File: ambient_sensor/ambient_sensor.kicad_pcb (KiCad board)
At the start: 2 copper layers, 69.5 x 54 mm, 22 parts, among them J1 Conn_01x02_Pin, J2 Conn_01x02_Pin, J3 Conn_01x05_Pin, J4 Conn_01x01_Pin, J5 Conn_01x04_Pin, J6 Conn_01x02_Pin, U4 ATmega328-P, U6 LD1117S33TR_SOT223, Y1 Crystal

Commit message: everything connected but warnings
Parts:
- moved U2 157.6 mm to (248.7, 132.6), turned to 180 degrees
- moved C1 144.3 mm to (219.1, 109.2)
- moved C2 144.3 mm to (213.7, 109.2)
- moved J1 140.7 mm to (245.1, 115.5)
- moved J2 140.7 mm to (236.6, 114.2)
- moved J3 140.7 mm to (208.6, 129.8)
- moved J4 140.7 mm to (208.6, 114.8)
- moved J5 140.7 mm to (228.6, 129.8)
- moved J6 140.7 mm to (229.1, 114.2)
- moved R2 140.7 mm to (245.1, 122.3)
- moved U4 140.7 mm to (241.6, 118.0)
- moved U7 140.7 mm to (159.2, 107.7)
- moved Y1 140.7 mm to (214.1, 113.8)
- moved BT1 136.6 mm to (258.9, 137.6)
- moved C5 136.6 mm to (263.4, 127.1)
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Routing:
- net GND: track 28.1 -> 91.2 mm, vias 2 -> 1
- net +5V: track 154.7 -> 179.0 mm, vias 3 -> 1
- net SCL: track 81.0 -> 56.7 mm, vias 2 -> 0
- net SDA: track 67.3 -> 44.8 mm
- net /CS: track 16.8 -> 15.4 mm
- net Net-(U4-XTAL1/PB6): track 13.5 -> 14.5 mm

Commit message: almost all errors
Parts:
- moved J1 2.55 mm to (245.0, 118.0), turned to 180 degrees
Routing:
- net RST: track 10.7 -> 14.4 mm
- net +5V: track 179.0 -> 175.7 mm, vias 1 -> 2
- net GND: track 91.2 -> 88.7 mm
- net SCL: track 56.7 -> 57.2 mm

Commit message: almost all warnings
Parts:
- added REF**: MountingHole_2.2mm_M2, MountingHole:MountingHole_2.2mm_M2, F.Cu at (227.9, 141.8)
- added REF**: MountingHole_2.2mm_M2, MountingHole:MountingHole_2.2mm_M2, F.Cu at (166.1, 141.8)
- added REF**: MountingHole_2.2mm_M2, MountingHole:MountingHole_2.2mm_M2, F.Cu at (228.9, 94.5)
- moved U7 116.0 mm to (271.2, 138.1), turned to 0 degrees
- moved REF** 107.3 mm to (165.9, 94.2), turned to 180 degrees
- moved D1 102.0 mm to (165.0, 113.8), turned to 90 degrees
- moved C5 96.8 mm to (167.0, 118.7), turned to 0 degrees
- moved C4 96.5 mm to (167.0, 121.2), turned to 0 degrees
- moved R1 96.2 mm to (168.0, 113.7), turned to 90 degrees
- moved BT1 92.3 mm to (171.5, 108.1), turned to 0 degrees
- moved U6 82.8 mm to (174.0, 118.7), turned to 0 degrees
- moved U2 69.8 mm to (181.7, 113.1), turned to 0 degrees
- moved J1 60.4 mm to (185.4, 127.7), turned to 0 degrees
- moved R2 59.9 mm to (185.3, 123.5), turned to 90 degrees
- moved U1 56.2 mm to (220.5, 95.3), turned to 180 degrees
- moved U4 53.8 mm to (188.8, 127.8), turned to 90 degrees
- moved J2 46.2 mm to (193.8, 131.5), turned to -90 degrees
- moved U3 36.7 mm to (198.8, 113.3), turned to 0 degrees
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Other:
- outline, holes or cut-outs redrawn
- board text added: "SGP30"

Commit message: no warnings
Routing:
- net unconnected-(U7-unknown-Pad2)_1: track 0.00 -> 2.50 mm
- net unconnected-(U7-unknown-Pad1)_1: track 0.00 -> 2.50 mm

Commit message: should be ok
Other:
- board text added: "École Centrale de Lille"
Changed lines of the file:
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@@
 		(layer "Edge.Cuts")
+	)
+	(gr_text "École\nCentrale\nde Lille"
+		(at 165 134 0)
+		(layer "F.Cu")
+		(effects
+			(font
+				(size 2 2)
+				(thickness 0.5)
+				(bold yes)
+			)
+			(justify left bottom)
+		)
 	)
 	(gr_text "SGP30"

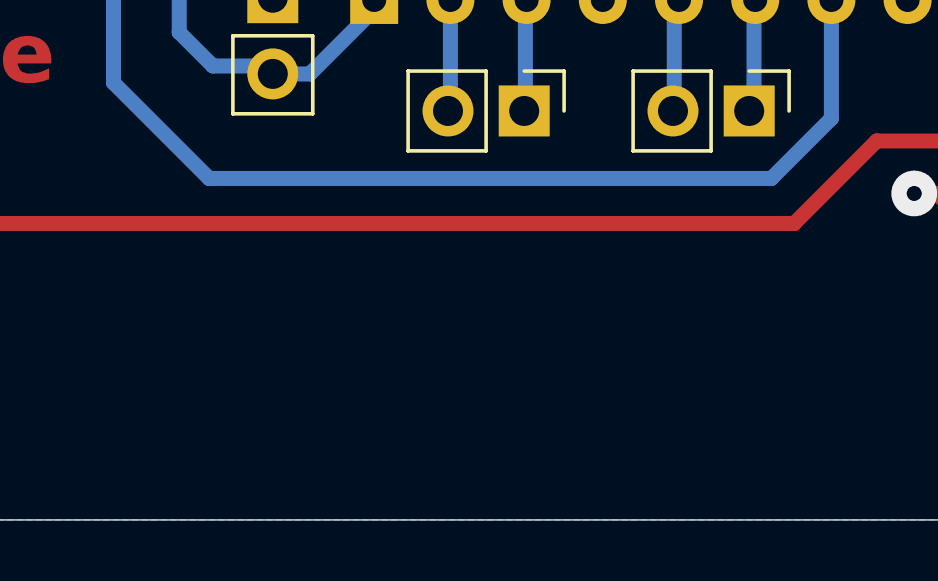
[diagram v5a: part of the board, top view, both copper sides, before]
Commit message: USB footprint
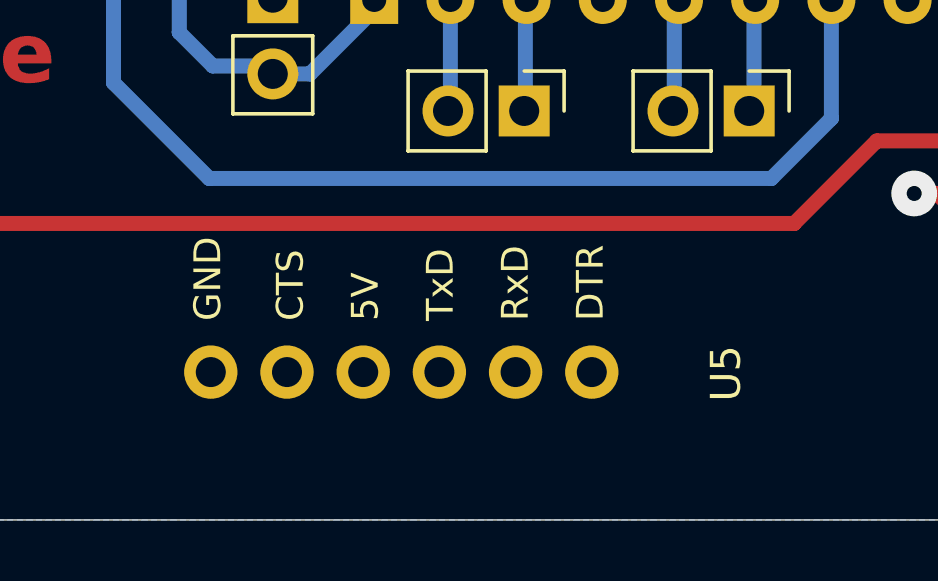
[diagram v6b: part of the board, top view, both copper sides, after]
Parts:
- added U5: ~, sensors:USB_FTDI_GT1125, F.Cu at (201.0, 140.2)
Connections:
- net Net-(J2-Pin_1) renamed /TX
- net Net-(J2-Pin_2) renamed /RX
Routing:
- net unconnected-(U7-unknown-Pad1)_1: track 0.00 -> 2.50 mm
- net unconnected-(U7-unknown-Pad1): track 2.50 -> 0.00 mm

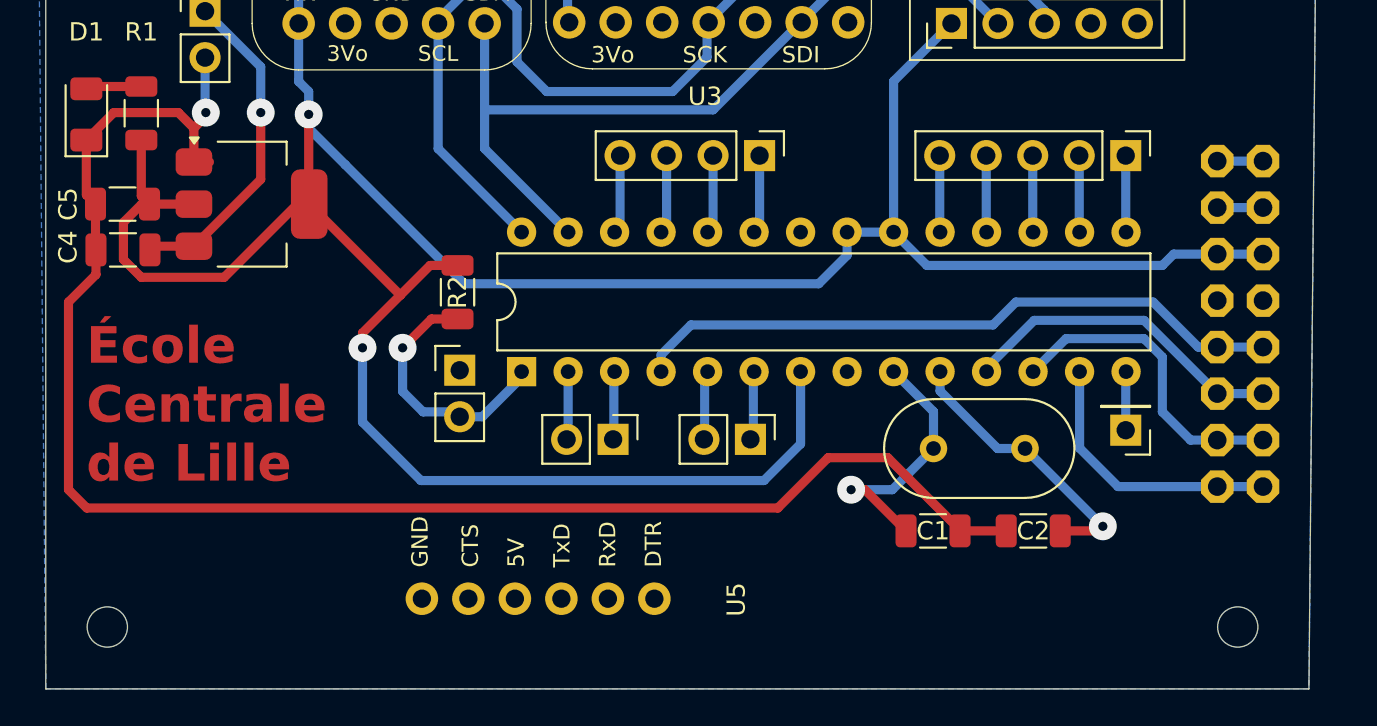
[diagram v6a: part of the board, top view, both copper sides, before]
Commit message: USB in the PCB
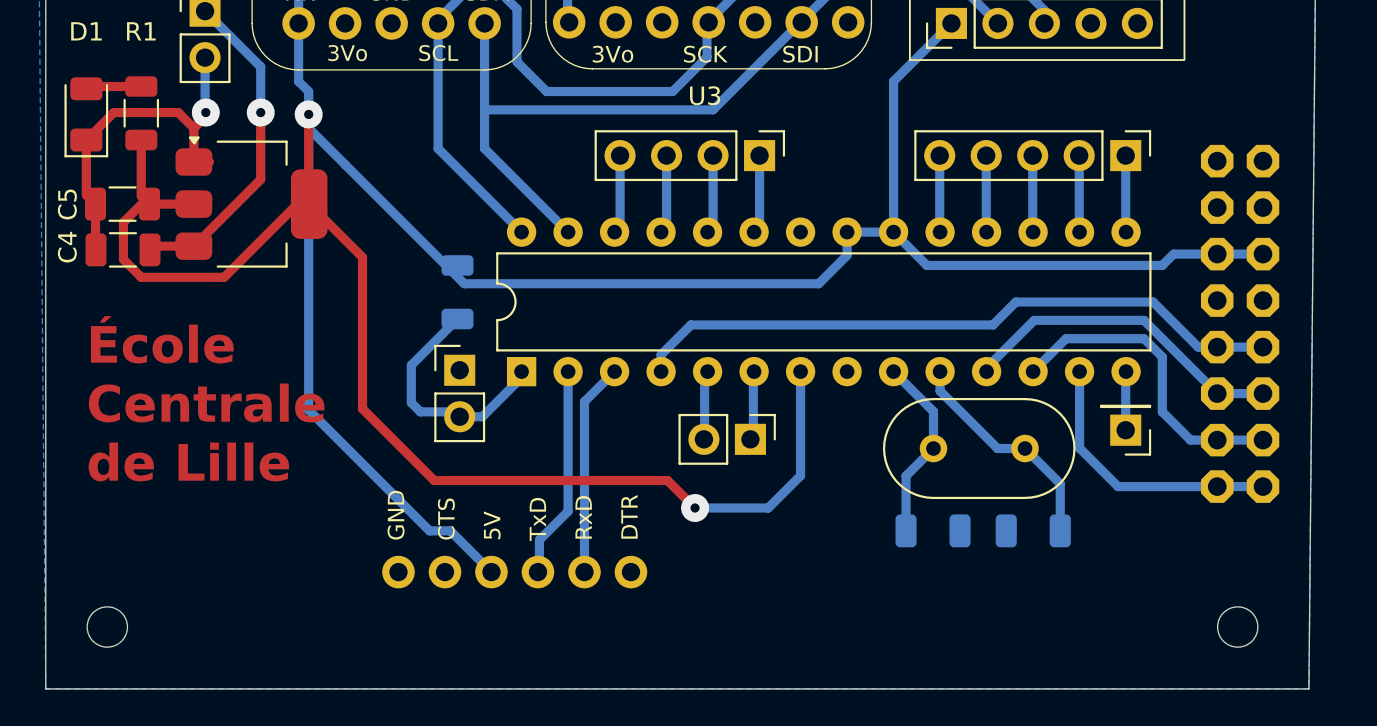
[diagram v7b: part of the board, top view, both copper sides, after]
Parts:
- removed J2: Conn_01x02_Pin, Connector_PinHeader_2.54mm:PinHeader_1x02_P2.54mm_Vertical
- C1, C2, R2: moved to B.Cu
- moved U5 1.94 mm to (199.7, 138.8)
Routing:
- net GND: track 88.7 -> 20.5 mm
- net +5V: track 175.7 -> 201.0 mm
- net /RX: track 3.22 -> 11.6 mm
- net /TX: track 3.22 -> 11.6 mm
- net Net-(U4-XTAL1/PB6): track 14.5 -> 10.2 mm, vias 1 -> 0
- net /CS: track 15.4 -> 12.3 mm, vias 1 -> 0
- net unconnected-(U7-unknown-Pad2)_1: track 2.50 -> 0.00 mm
- net unconnected-(U7-unknown-Pad1)_1: track 2.50 -> 0.00 mm
- net RST: track 14.4 -> 13.3 mm, vias 1 -> 0

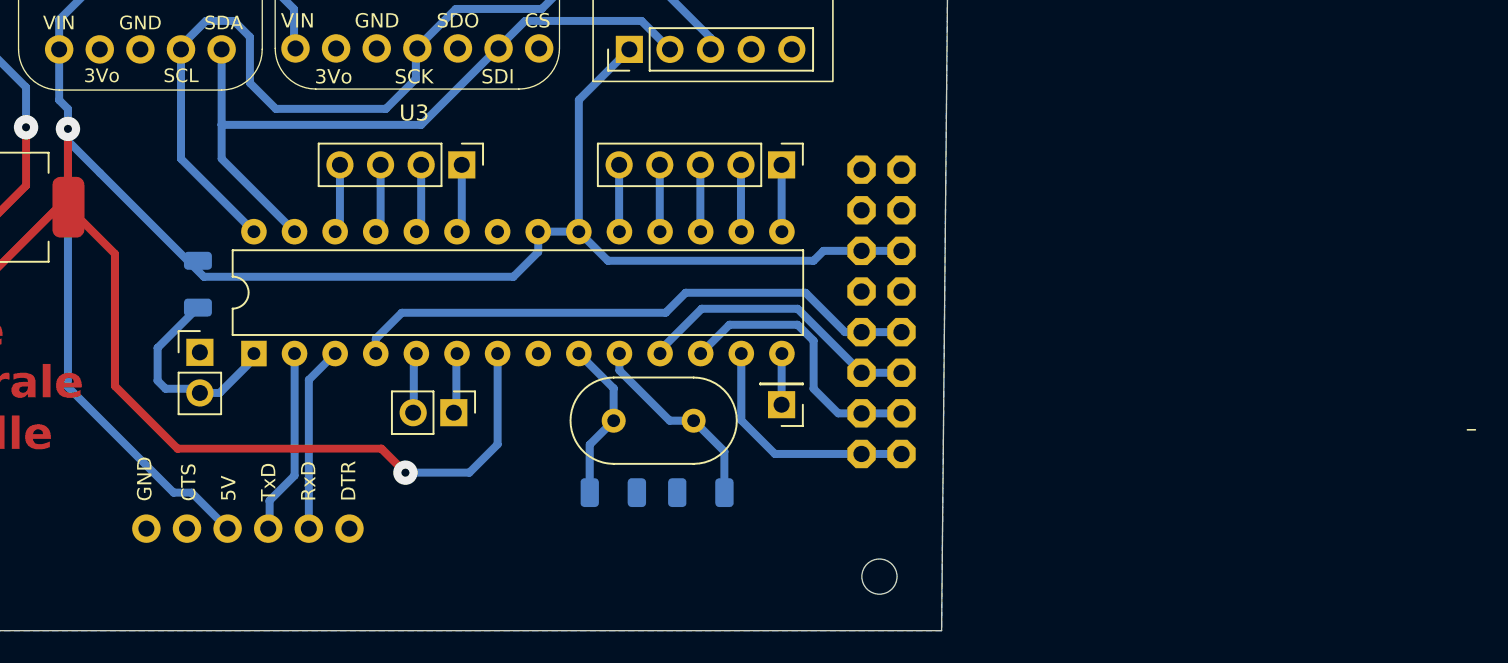
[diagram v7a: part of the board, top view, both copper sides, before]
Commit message: fixed sd card reader
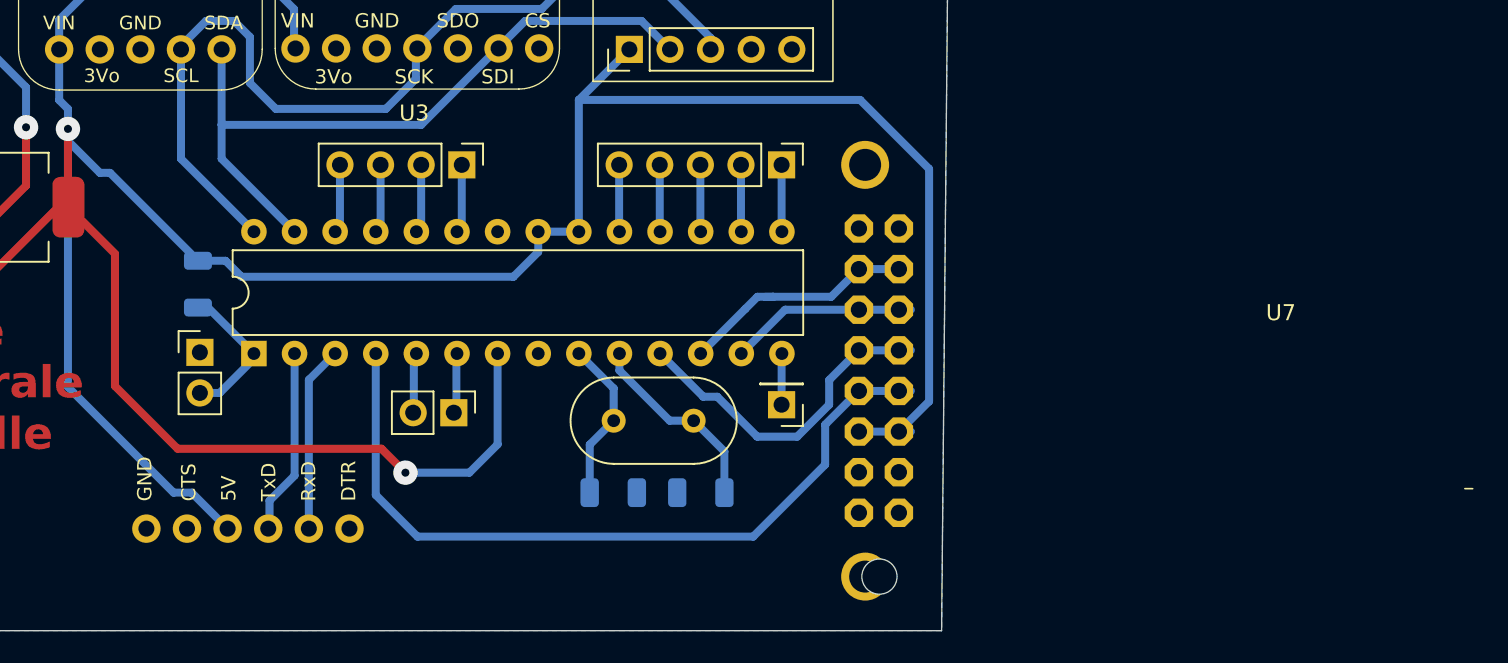
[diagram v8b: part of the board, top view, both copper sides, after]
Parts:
- moved U7 3.68 mm to (271.0, 141.8)
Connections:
- U7 pad 1: unconnected-(U7-unknown-Pad1) -> GND
- U7 pad 4: GND -> /DT
- U7 pad 5: /DT -> /MOSI
- U7 pad 6: /MOSI -> /CLK
- U7 pad 8: /CLK -> GND
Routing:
- net +5V: track 201.0 -> 223.2 mm
- net /DT: track 36.0 -> 47.9 mm
- net RST: track 13.3 -> 9.65 mm
- net /CLK: track 15.1 -> 11.7 mm
- net /MOSI: track 18.4 -> 20.8 mm
- net /MISO: track 17.4 -> 15.1 mm
